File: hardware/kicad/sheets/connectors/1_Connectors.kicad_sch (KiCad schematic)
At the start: 26 parts, among them CN6 5017, Q14 CSD17577Q5A, U48 MT9700-N, U49 LM5050MKX-1/NOPB, U50 150uF, U51 DS1021-2x13SF11-B

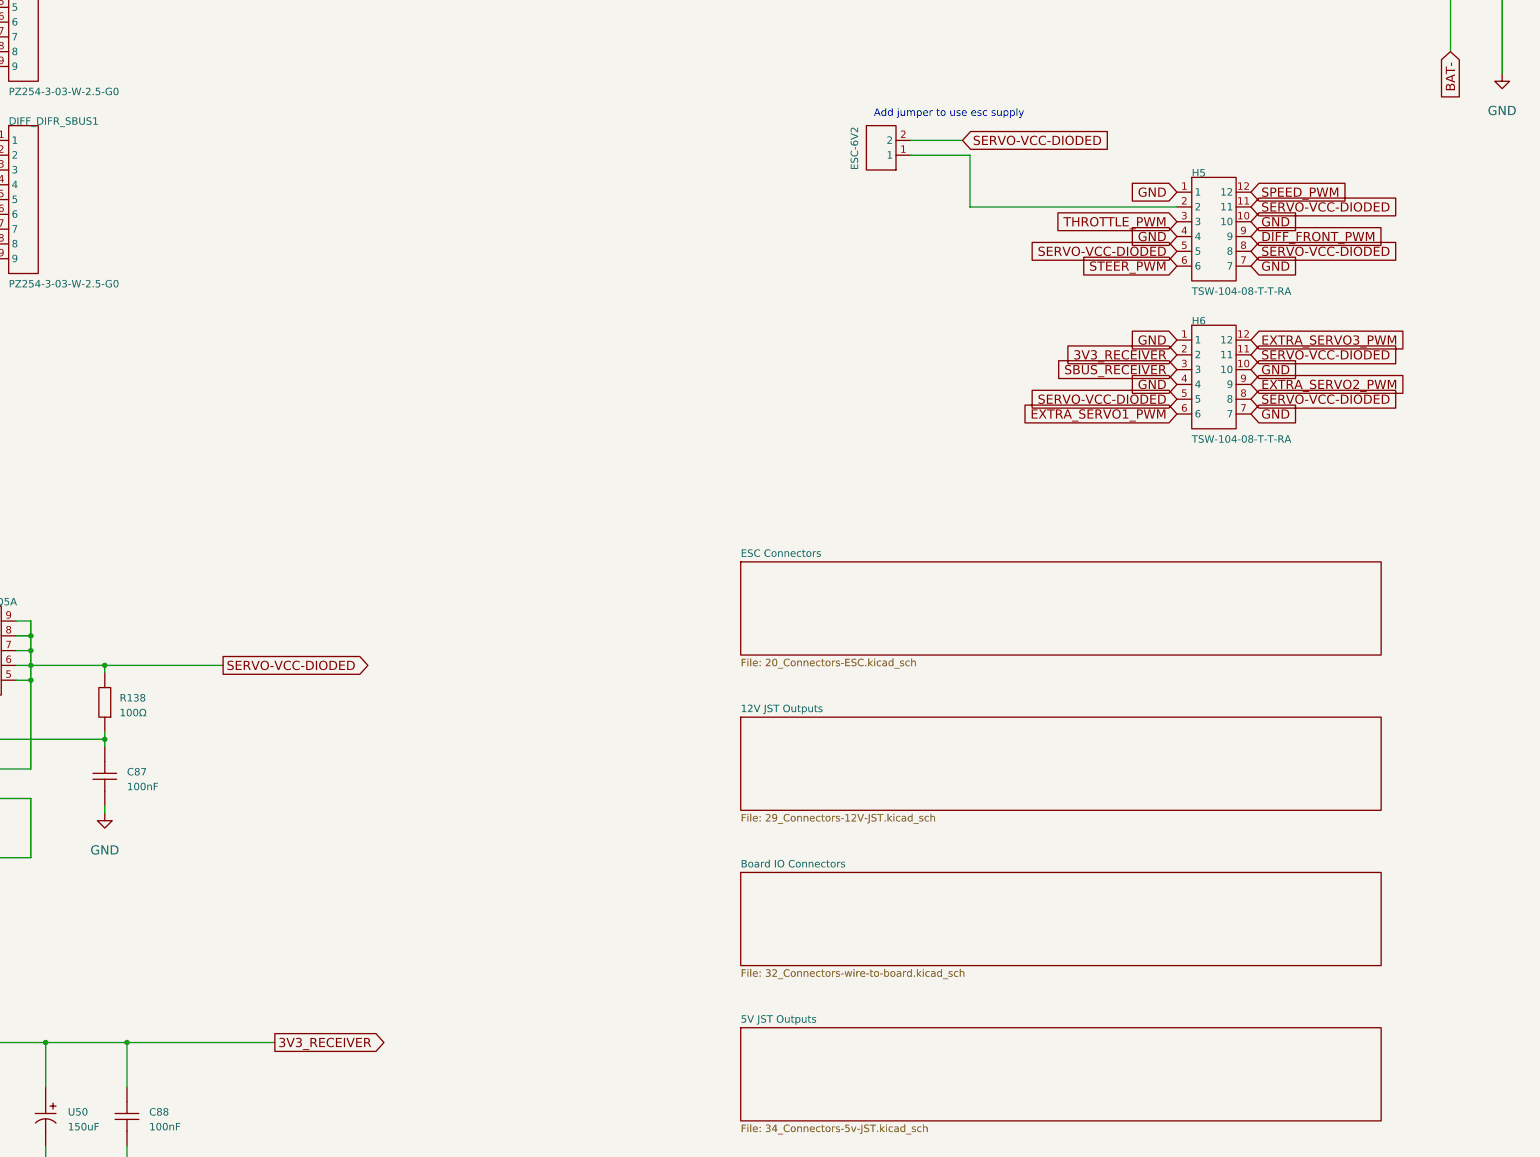
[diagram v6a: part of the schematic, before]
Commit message: netties and better sheet nesting for servo connectors
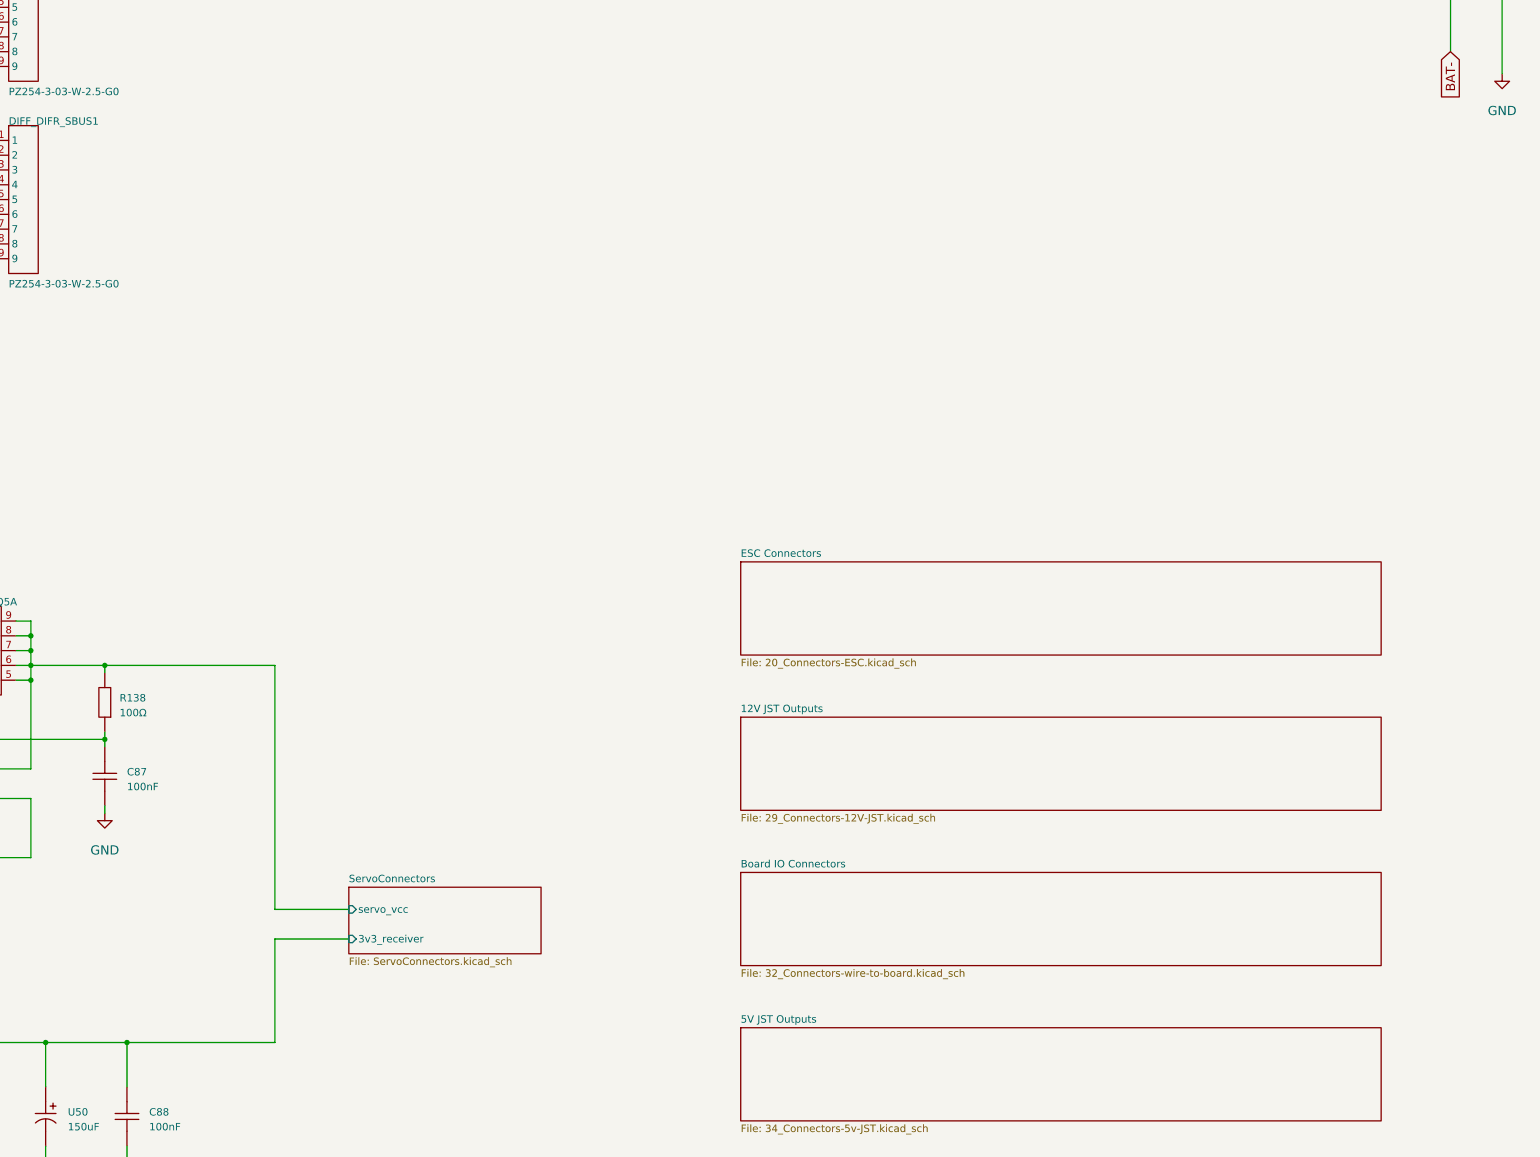
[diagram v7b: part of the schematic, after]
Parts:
- removed ESC-6V2: PZ254V-11-02P, Connector_PinHeader_2.54mm:PinHeader_1x02_P2.54mm_Vertical, symbol 5v rail sm-easyedapro:PZ254V-11-02P
- removed H5, H6: TSW-104-08-T-T-RA, 5v rail sm-easyedapro:HDR-TH_12P-P2.54-H-M-R3-C4_TSW-104-08-XXX-T-RA, symbol 5v rail sm-easyedapro:TSW-104-08-T-T-RA
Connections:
- net 3V3_RECEIVER renamed ServoConnectors/3v3_receiver
- net SERVO-VCC-DIODED renamed ServoConnectors/servo_vcc
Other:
- added sheet ServoConnectors (ServoConnectors.kicad_sch)
- note removed: "Add jumper to use esc supply"

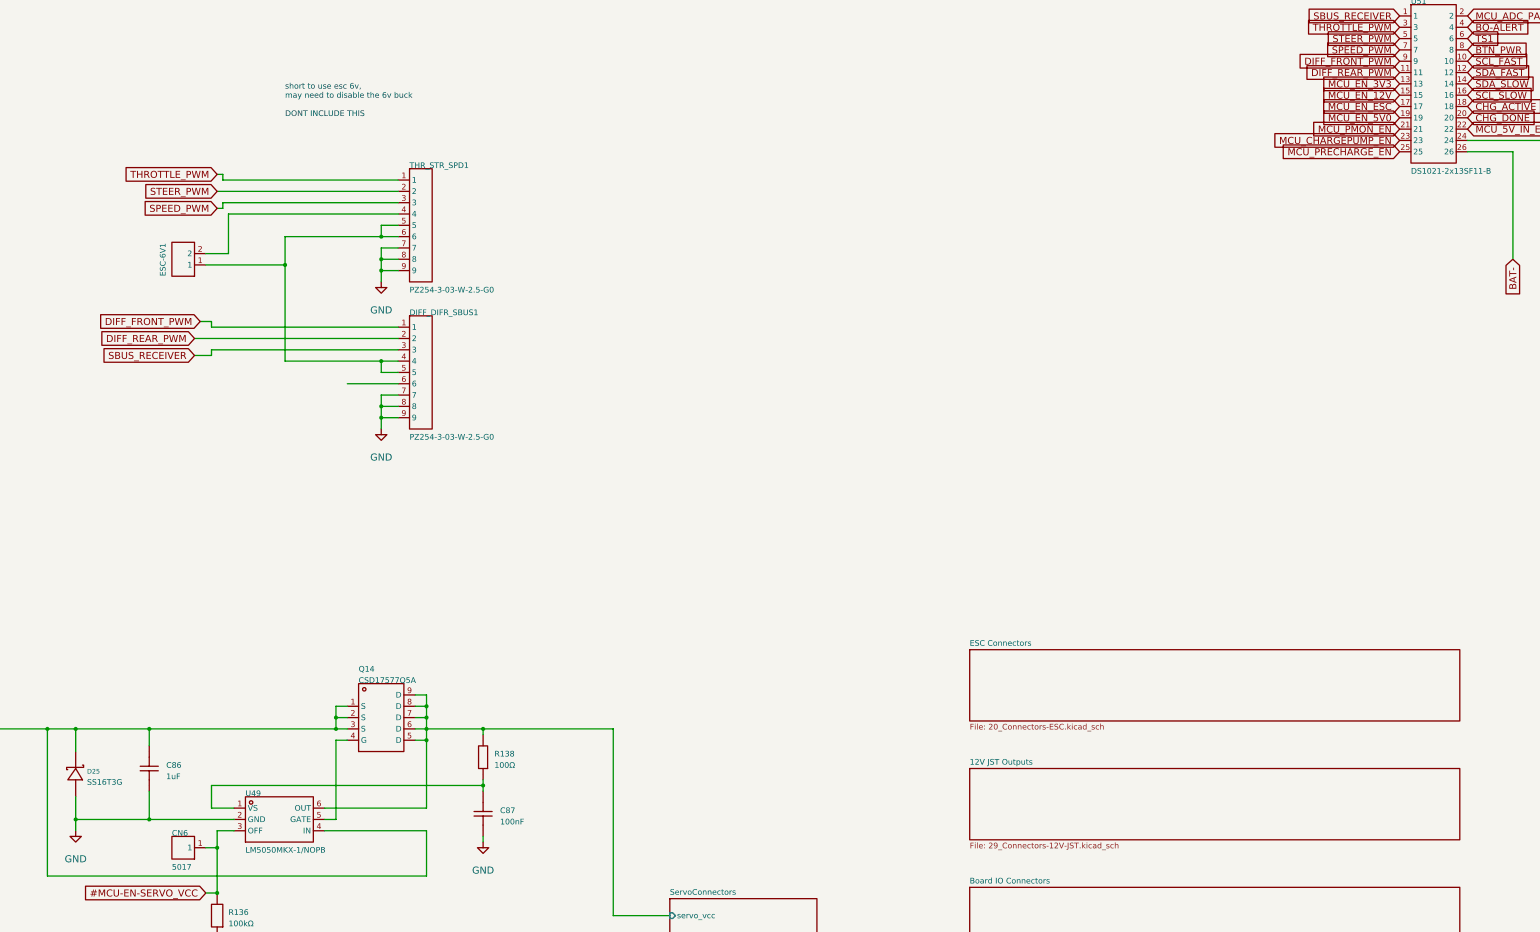
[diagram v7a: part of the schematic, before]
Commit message: more sheet simplfiication and pre simpler 12v sym
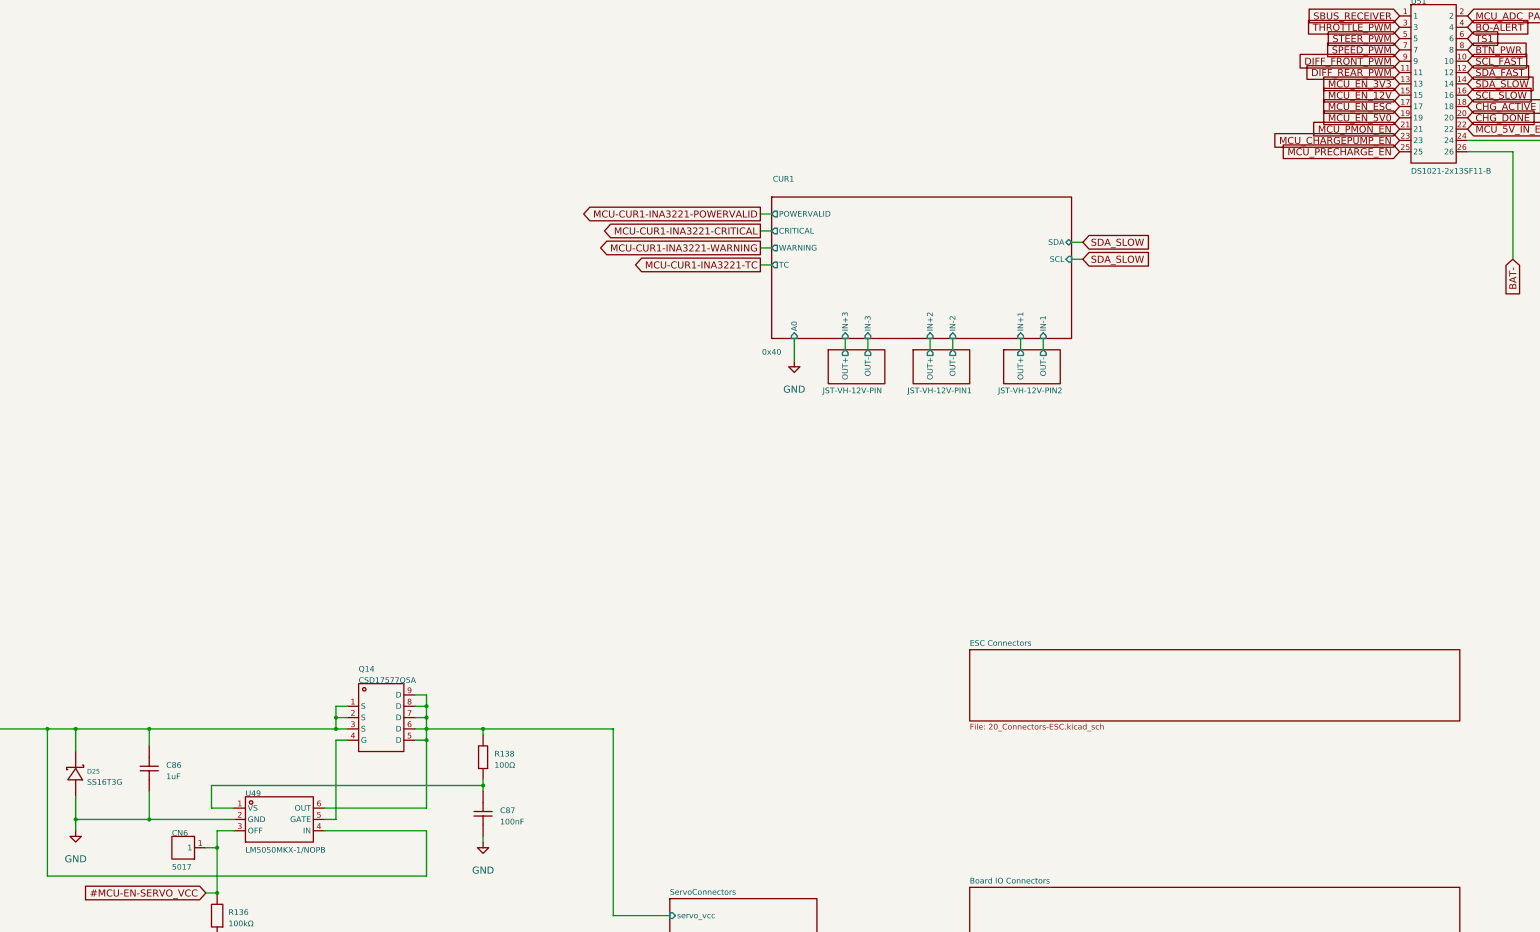
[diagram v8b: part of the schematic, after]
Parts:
- removed DIFF_DIFR_SBUS1, THR_STR_SPD1: PZ254-3-03-W-2.5-G0, Connector_PinHeader_2.54mm:PinHeader_1x09_P2.54mm_Vertical, symbol 5v rail sm-easyedapro:PZ254-3-03-W-2.5-G0
- removed ESC-6V1: PZ254V-11-02P, Connector_PinHeader_2.54mm:PinHeader_2x01_P2.54mm_Vertical, symbol 5v rail sm-easyedapro:PZ254V-11-02P
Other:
- removed sheet 12V JST Outputs
- added sheet CUR1 (MISC_IO_CURR_SENSING_1.kicad_sch)
- added sheet JST-VH-12V-PIN (JST-VH-12V-PIN.kicad_sch)
- added sheet JST-VH-12V-PIN1 (JST-VH-12V-PIN.kicad_sch)
- added sheet JST-VH-12V-PIN2 (JST-VH-12V-PIN.kicad_sch)
- note removed: "short to use esc 6v, may need to disable the 6v buck DONT INCLUDE THIS"
